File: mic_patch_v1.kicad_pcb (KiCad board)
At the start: 2 copper layers, 30 x 30 mm, 25 parts, among them J1 Conn_ARM_SWD_TagConnect_TC203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, U1 NORA-B106-00B, U2 PWR_nPM1100-QDXX, U3 ADAU7002ACBZ-R7, Y1 CLK_0003

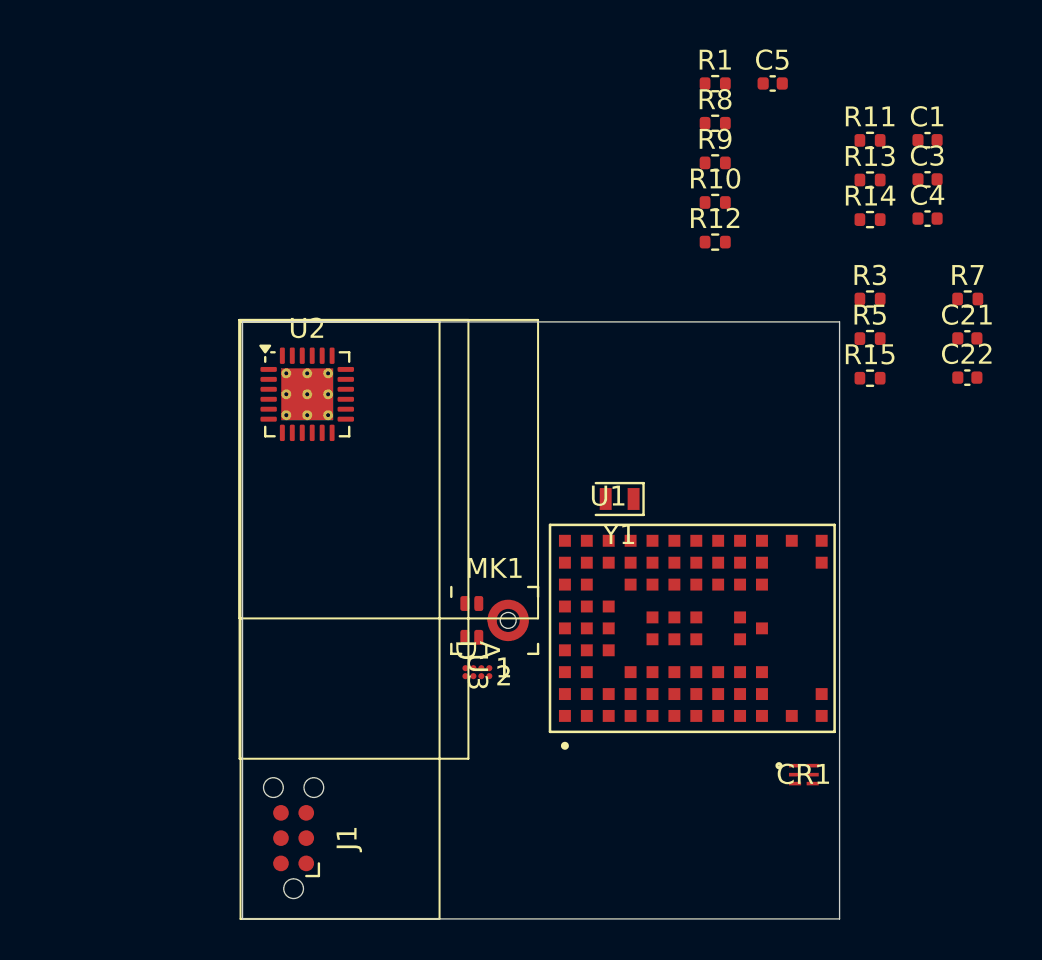
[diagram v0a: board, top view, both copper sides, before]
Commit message: added SMD indicator LED symbol & footprint
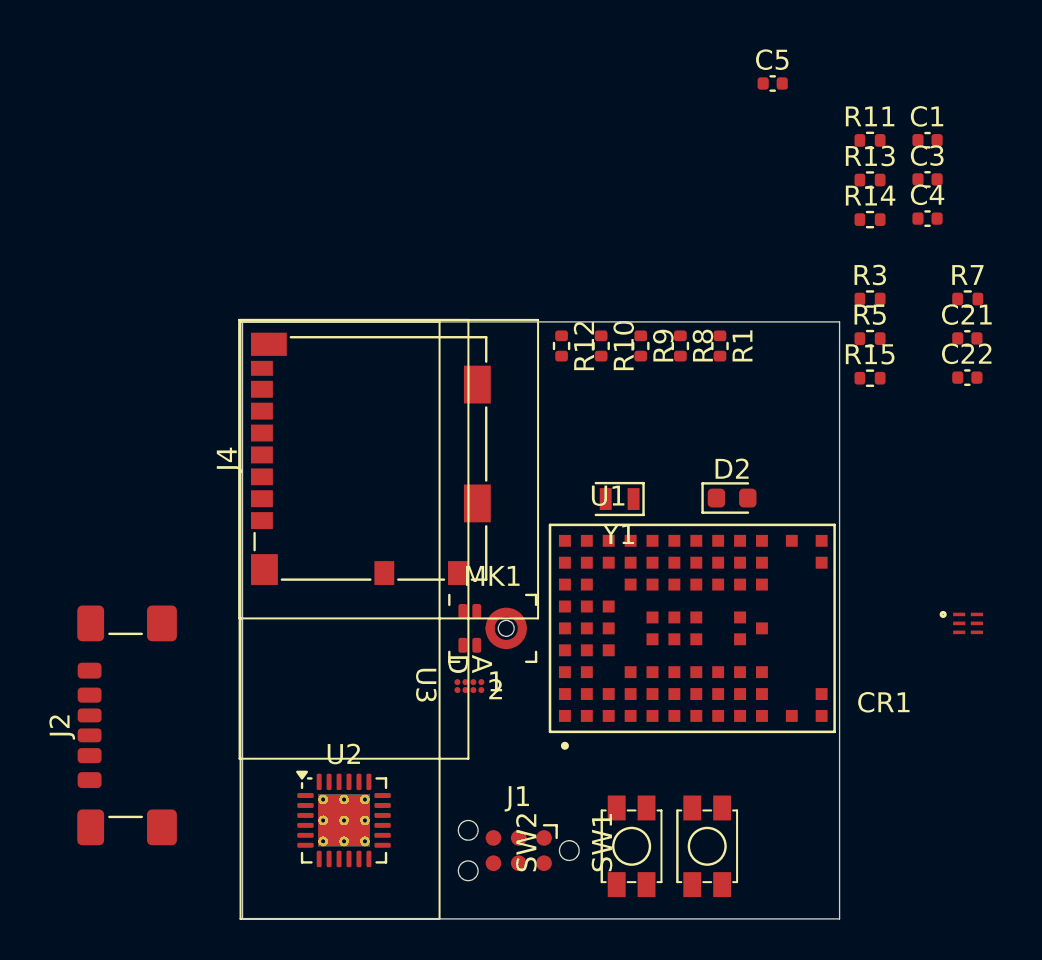
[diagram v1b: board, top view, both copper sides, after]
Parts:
- added D2: LED_0002, LED_SMD:LED_0603_1608Metric, F.Cu at (118.3, 69.8)
- added J2: J_000001, Connector_USB:USB_C_Receptacle_GCT_USB4135-GF-A_6P_TopMnt_Horizontal, F.Cu at (89.0, 81.2)
- added J4: Micro_SD_Card, Connector_Card:microSD_HC_Molex_104031-0811, F.Cu at (100.1, 67.8)
- added SW1: SW_000001, mic_patch_parts:SW_000001, F.Cu at (117.0, 87.2)
- added SW2: SW_000001, mic_patch_parts:SW_000001, F.Cu at (113.2, 87.2)
- moved U2 21.5 mm to (98.8, 86.0)
- moved R1 13.2 mm to (117.7, 62.1), turned to -90 degrees
- moved J1 11.3 mm to (107.6, 87.5), turned to 180 degrees
- moved R8 11.3 mm to (115.7, 62.1), turned to -90 degrees
- moved CR1 11.2 mm to (130.2, 76.0)
- moved R9 9.93 mm to (113.7, 62.1), turned to -90 degrees
- moved R12 9.32 mm to (109.7, 62.1), turned to -90 degrees
- moved R10 9.21 mm to (111.7, 62.1), turned to -90 degrees
- moved U3 0.81 mm to (105.1, 79.2)
- moved MK1 0.41 mm to (106.3, 76.3)

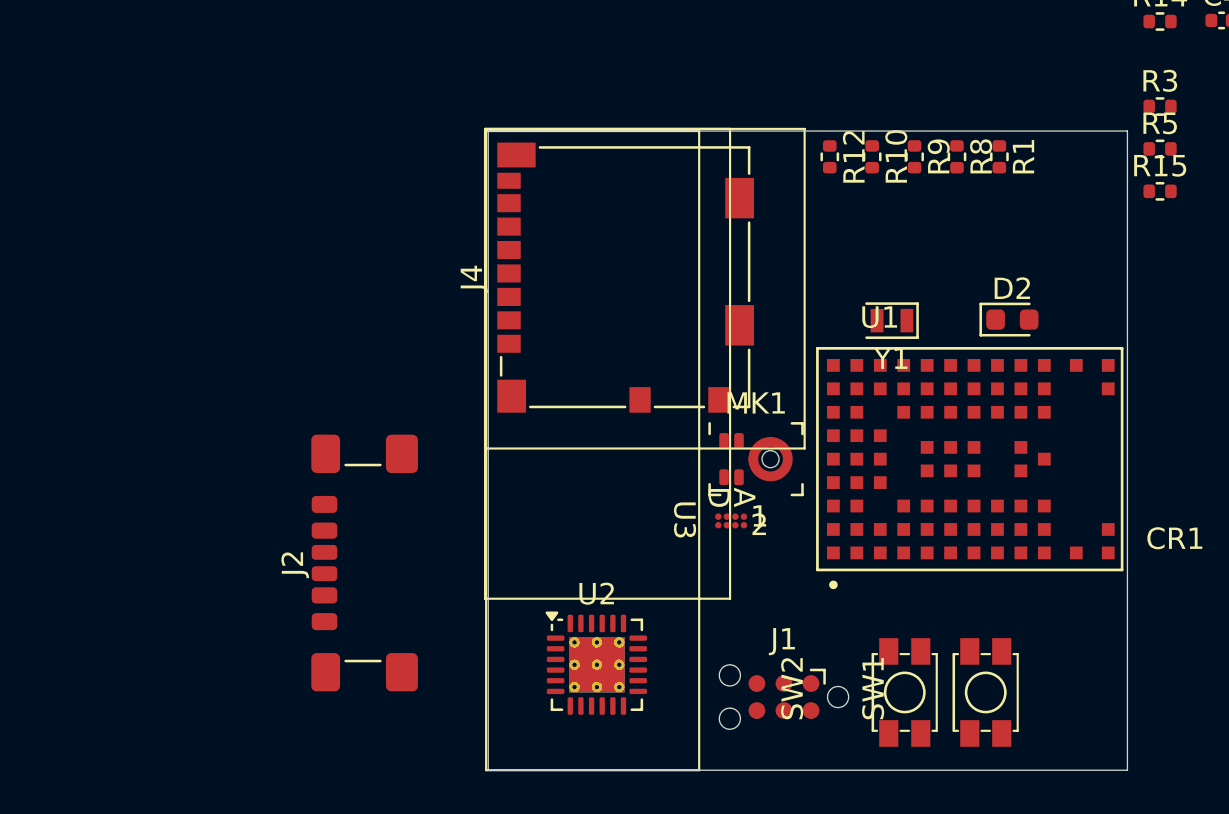
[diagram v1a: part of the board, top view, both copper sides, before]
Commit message: added JST connector symbol + footprint
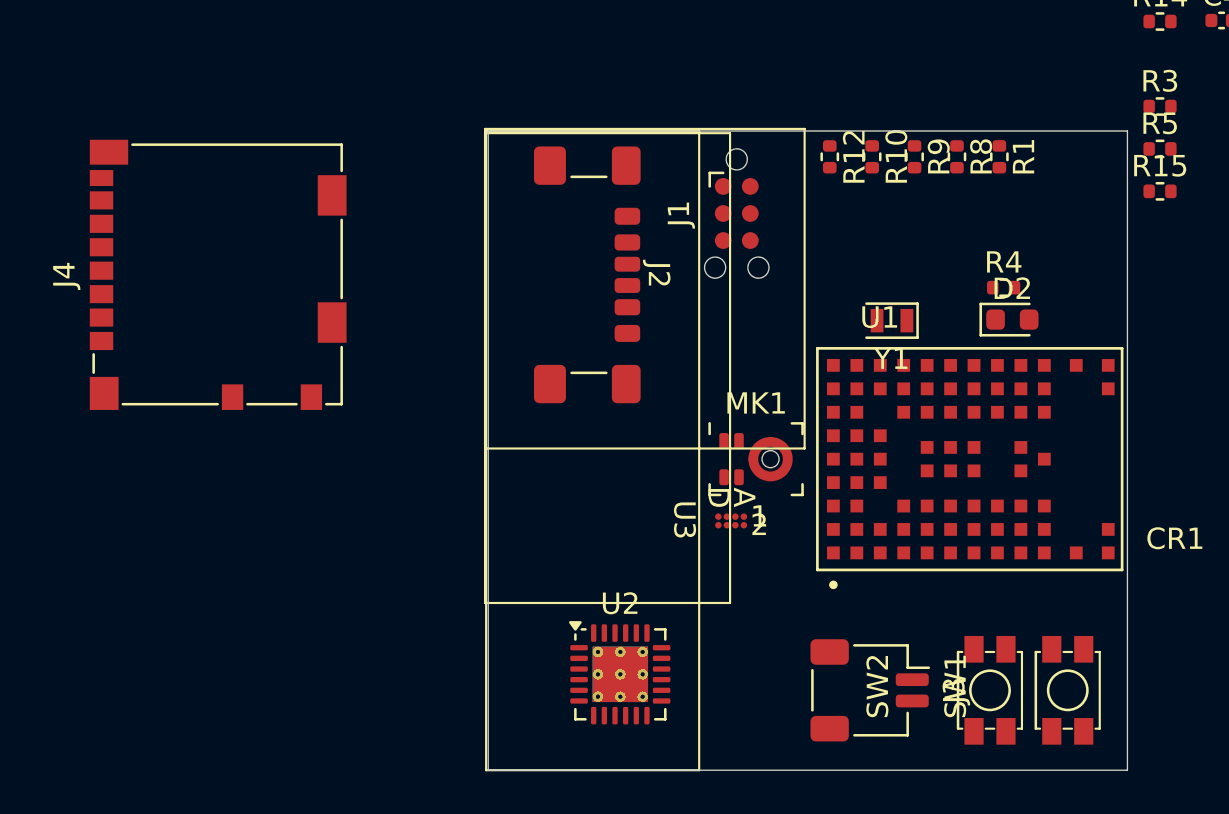
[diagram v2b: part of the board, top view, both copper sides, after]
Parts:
- added J3: J_000001, mic_patch_parts:J_000001, F.Cu at (111.6, 87.2)
- added R4: R_00004, Resistor_SMD:R_0402_1005Metric, F.Cu at (117.9, 68.2)
- moved J1 22.8 mm to (105.4, 64.8), turned to -90 degrees
- moved J4 19.1 mm to (81.0, 67.7)
- moved J2 15.8 mm to (97.2, 67.7), turned to -90 degrees
- moved SW2 4.00 mm to (117.2, 87.2)
- moved SW1 3.85 mm to (120.9, 87.2)
- moved U2 1.19 mm to (99.9, 86.4)

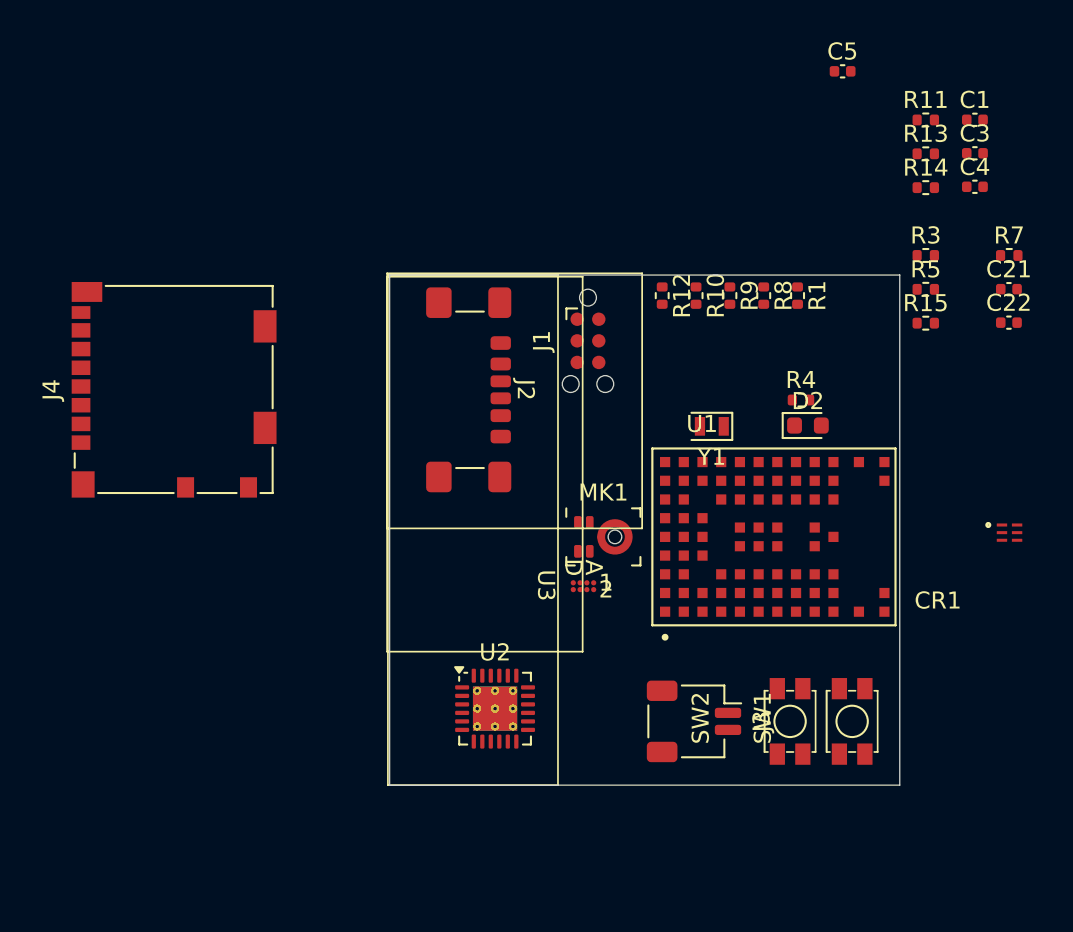
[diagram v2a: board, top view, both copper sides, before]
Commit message: added all footprints for power module
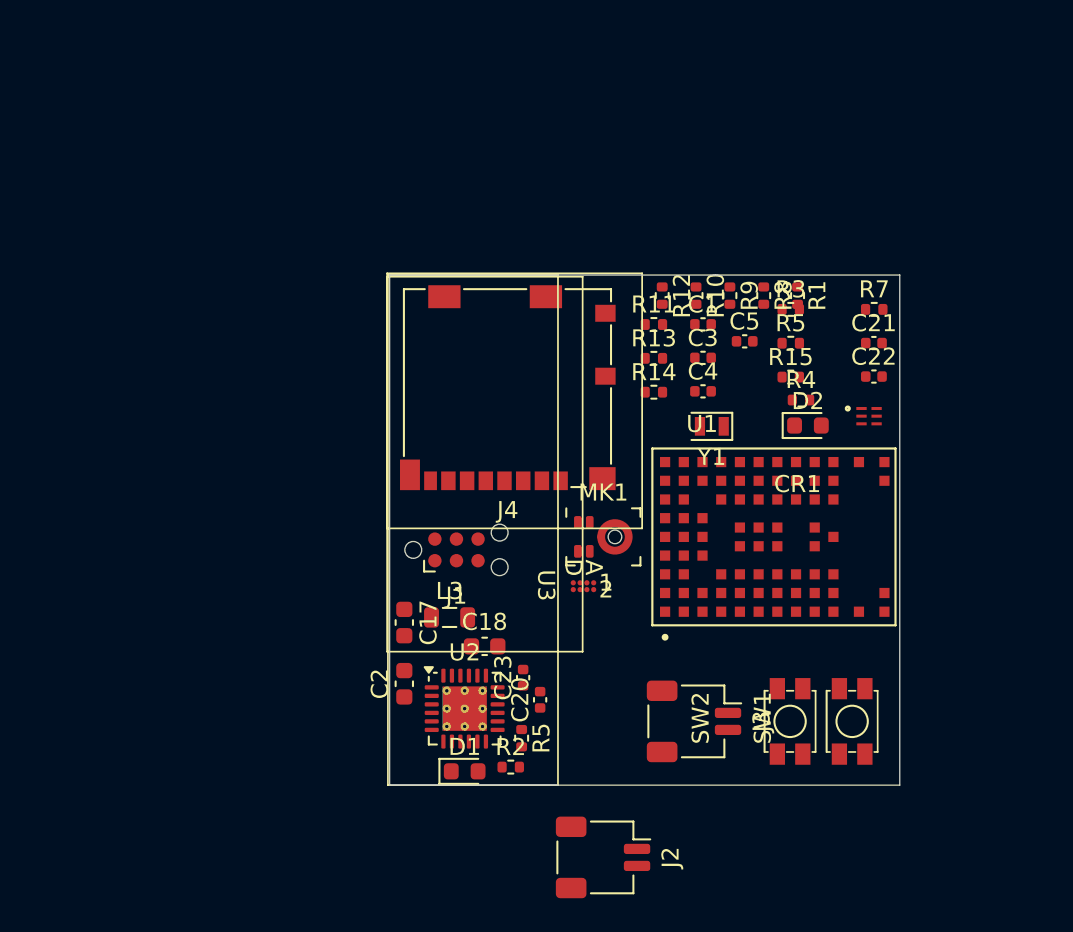
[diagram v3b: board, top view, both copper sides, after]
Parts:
- added C17: C_00005, Capacitor_SMD:C_0603_1608Metric, F.Cu at (94.6, 81.3)
- added C18: C_00005, Capacitor_SMD:C_0603_1608Metric, F.Cu at (99.3, 82.7)
- added C2: C_00005, Capacitor_SMD:C_0603_1608Metric, F.Cu at (94.6, 84.9)
- added C20: C_00003, Capacitor_SMD:C_0402_1005Metric, F.Cu at (102.5, 85.9)
- added C23: C_00003, Capacitor_SMD:C_0402_1005Metric, F.Cu at (101.5, 84.6)
- added D1: LED_0001, LED_SMD:LED_0603_1608Metric, F.Cu at (98.1, 90.1)
- added L3: L_00002, Inductor_SMD:L_0805_2012Metric, F.Cu at (97.2, 81.0)
- added R2: R_00002, Resistor_SMD:R_0402_1005Metric, F.Cu at (100.8, 89.8)
- added R5: R_00004, Resistor_SMD:R_0402_1005Metric, F.Cu at (101.5, 88.1)
- J2: footprint Connector_USB:USB_C_Receptacle_GCT_USB4135-GF-A_6P_TopMnt_Horizontal -> mic_patch_parts:J_000001
- moved J2 29.0 mm to (106.2, 95.2)
- moved R14 20.0 mm to (109.2, 67.8)
- moved R11 20.0 mm to (109.2, 63.8)
- moved C1 20.0 mm to (112.1, 63.8)
- moved C3 20.0 mm to (112.1, 65.8)
- moved C4 20.0 mm to (112.1, 67.7)
- moved R13 20.0 mm to (109.2, 65.8)
- moved J4 19.7 mm to (100.7, 67.5), turned to 180 degrees
- moved C5 16.9 mm to (114.6, 64.8)
- moved J1 14.5 mm to (97.6, 77.1), turned to 0 degrees
- moved CR1 10.7 mm to (121.9, 69.2)
- moved C21 8.55 mm to (122.2, 64.9)
- moved R15 8.55 mm to (117.3, 66.9)
- moved C22 8.55 mm to (122.2, 66.9)
- moved R3 8.55 mm to (117.3, 62.9)
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
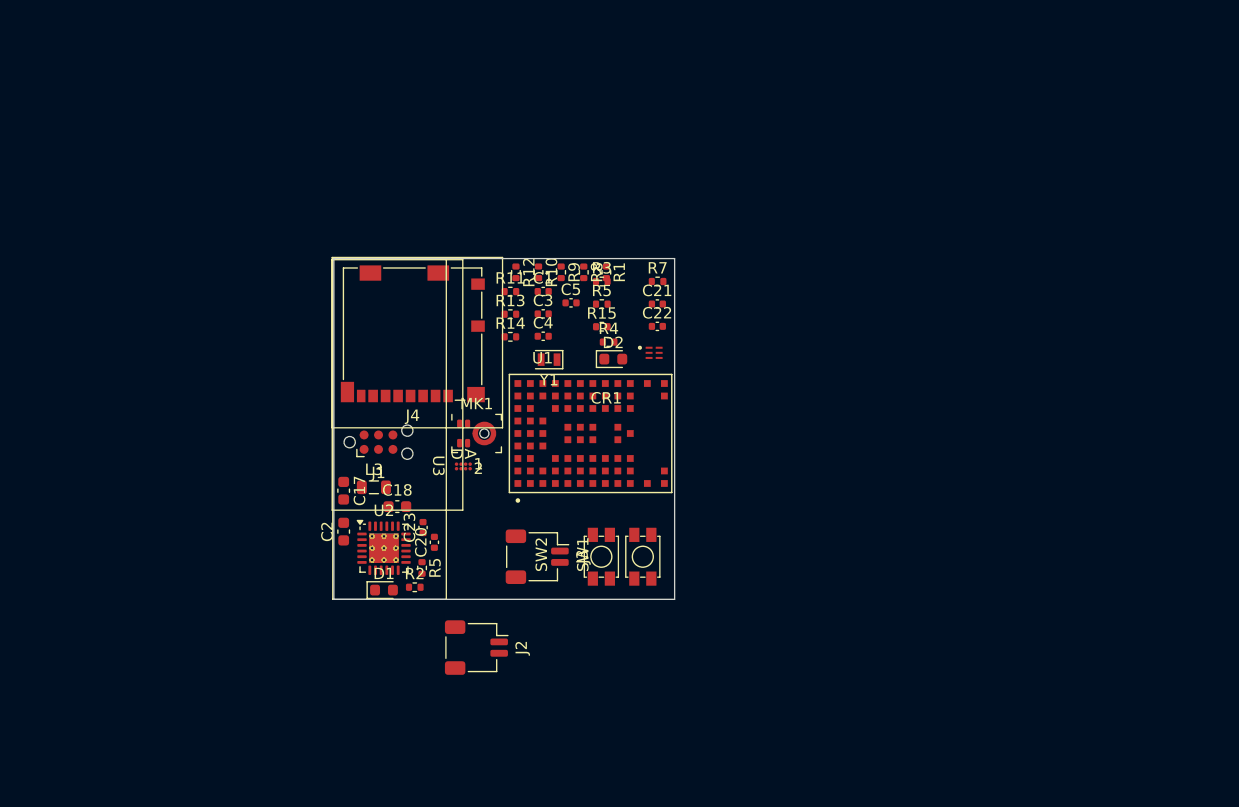
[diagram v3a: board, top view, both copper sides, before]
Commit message: Added USB symbol + 5.1k pull downs
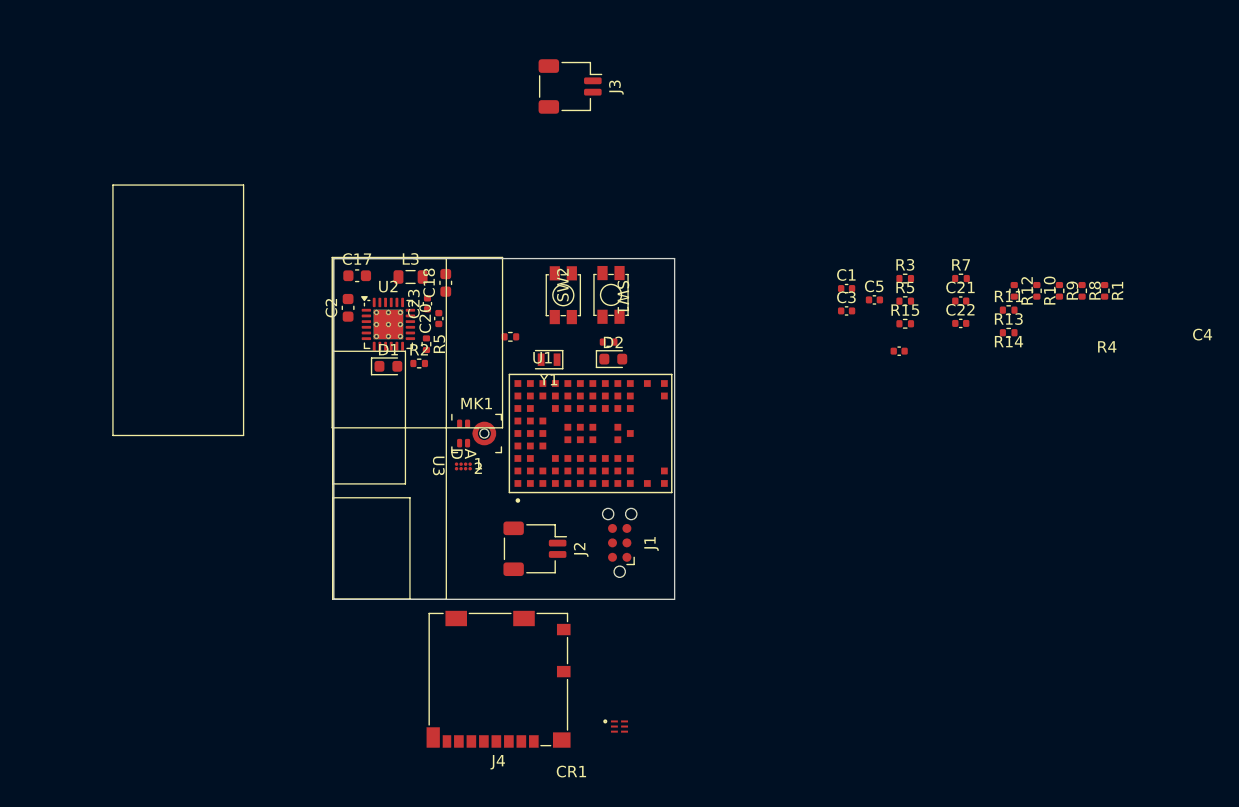
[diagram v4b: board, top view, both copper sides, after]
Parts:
- moved R11 43.9 mm to (153.1, 65.4)
- moved R13 43.9 mm to (153.1, 67.4)
- moved R9 43.9 mm to (157.6, 63.7)
- moved R1 43.9 mm to (161.6, 63.7)
- moved R10 43.9 mm to (155.6, 63.7)
- moved R12 43.9 mm to (153.6, 63.7)
- moved R8 43.9 mm to (159.6, 63.7)
- moved J3 41.5 mm to (114.5, 45.8)
- moved CR1 33.0 mm to (118.8, 102.1)
- moved C4 31.4 mm to (143.5, 69.0)
- moved J4 31.3 mm to (108.2, 98.0)
- moved C1 26.7 mm to (138.8, 63.5)
- moved C3 26.7 mm to (138.8, 65.5)
- moved C5 26.7 mm to (141.3, 64.5)
- moved R15 26.7 mm to (144.0, 66.6)
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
